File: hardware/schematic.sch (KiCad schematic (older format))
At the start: 21 parts, among them T1 CONN_4, T2 CONN_10, T3 CONN_1, U1 MSP430, U2 LM317

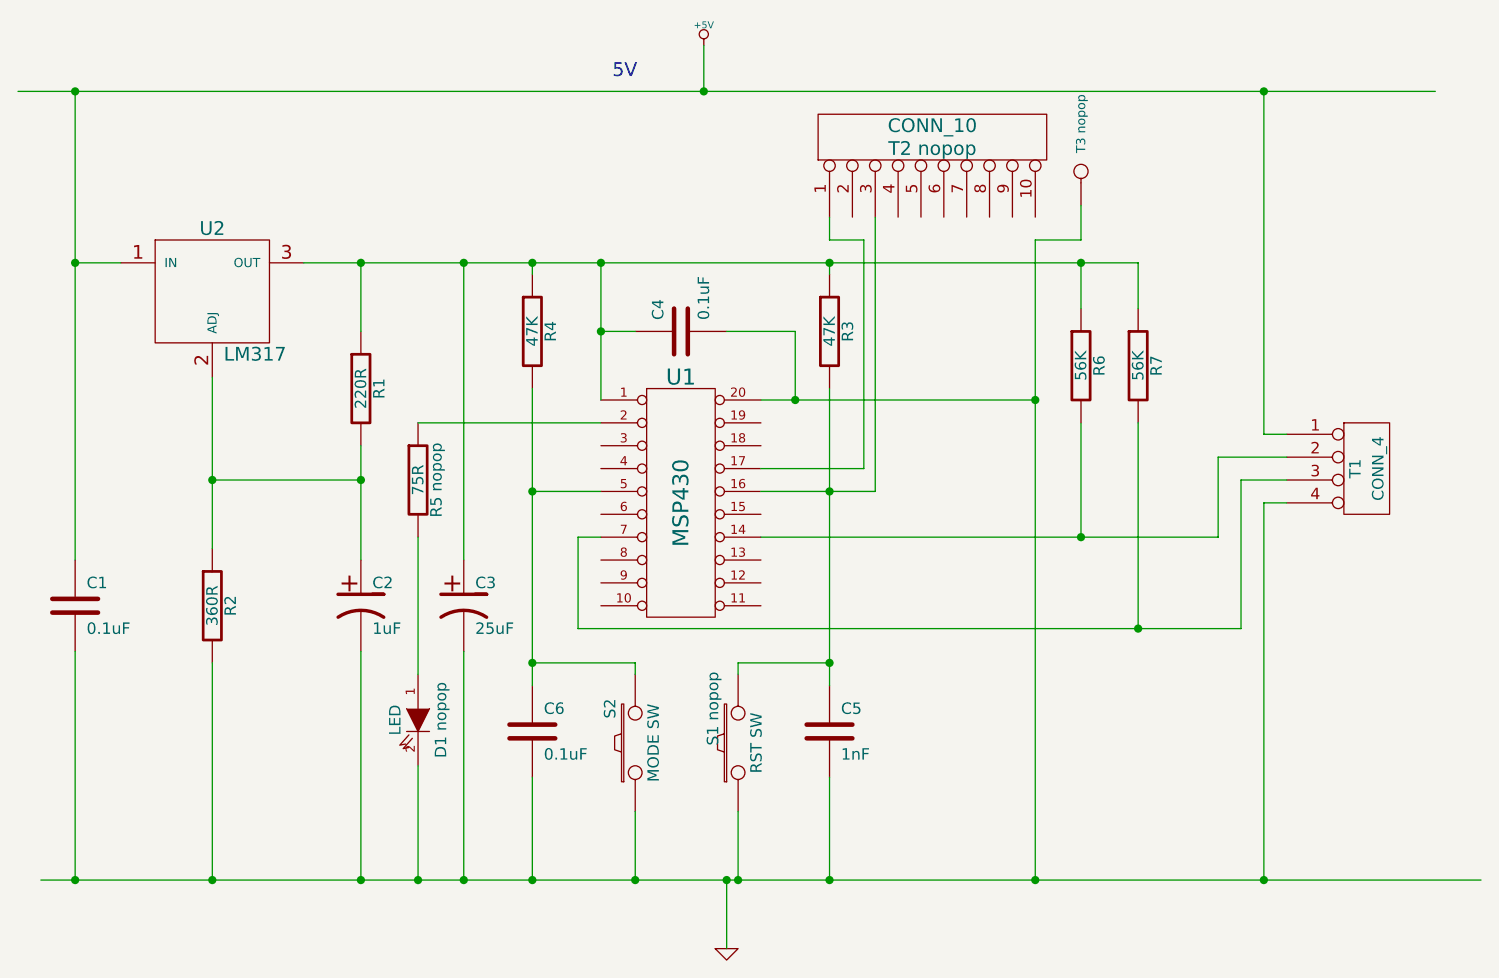
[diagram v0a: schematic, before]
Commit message: Add veroboard Layout
It's a spreadsheet, hardware is now tested and working.
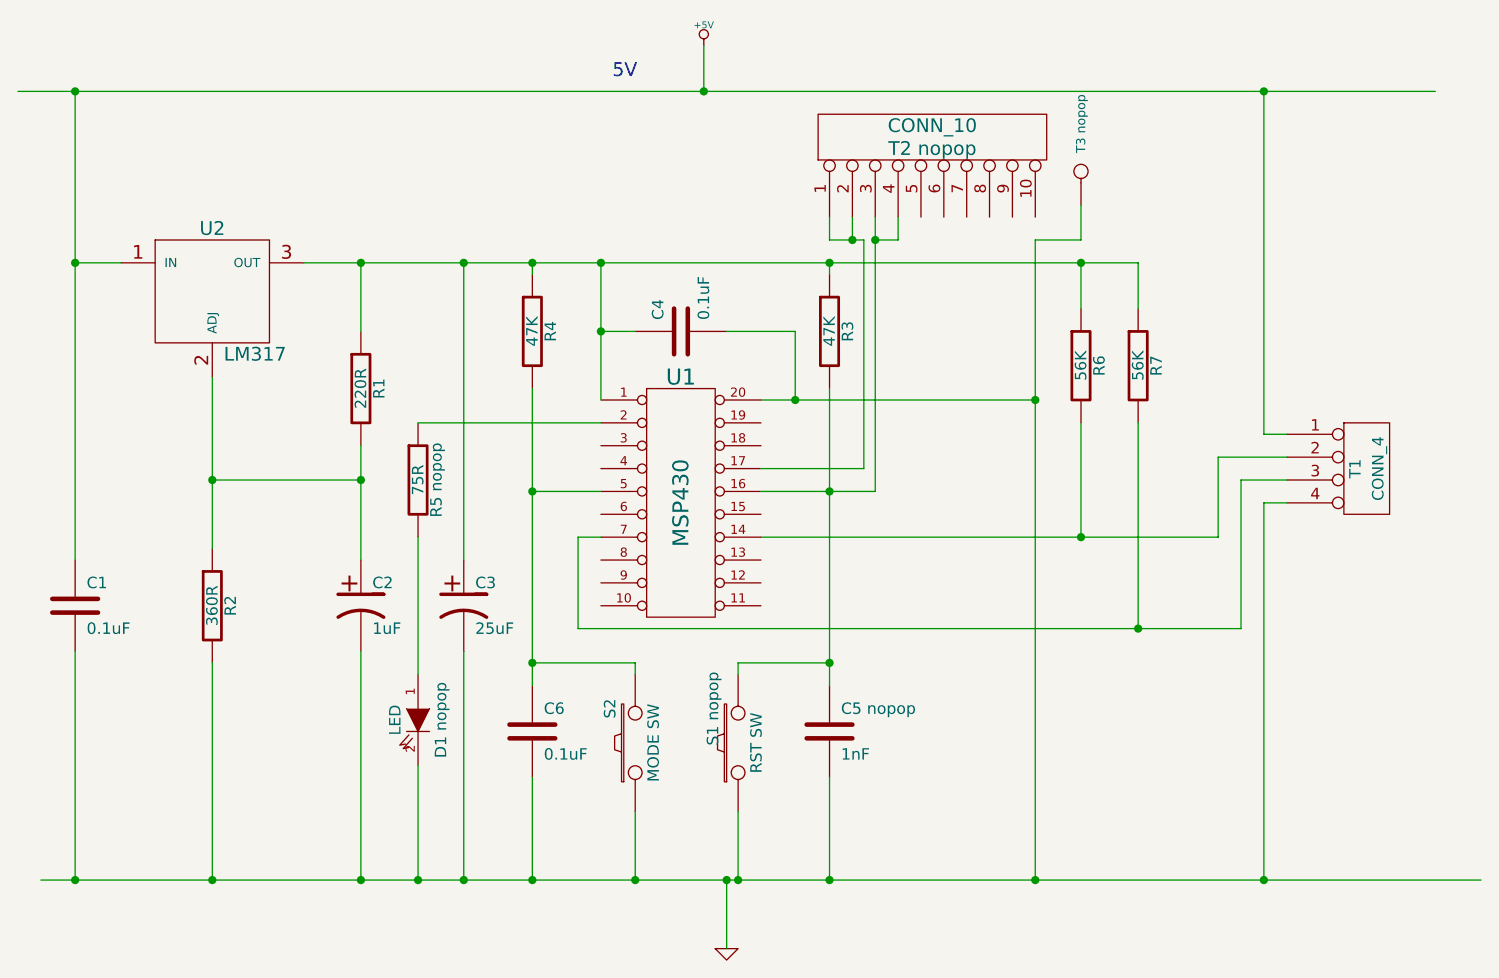
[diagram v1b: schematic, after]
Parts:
- renumbered C5 to C5~nopop, D1 to D1~nopop, R5 to R5~nopop, S1 to S1~nopop, T2 to T2~nopop, T3 to T3~nopop
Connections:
- wire segments 62 -> 65
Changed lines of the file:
@@
-EESchema Schematic File Version 2  date Thu 20 Dec 2012 17:31:51 GMT
+EESchema Schematic File Version 2  date Thu 20 Dec 2012 18:24:55 GMT
 LIBS:power
 LIBS:device
@@
 LIBS:contrib
 LIBS:valves
+LIBS:schematic-cache
 EELAYER 25  0
 EELAYER END
@@
 Comment4 ""
 $EndDescr
+Connection ~ 4650 1500
+Wire Wire Line
+	4650 1500 4750 1500
+Wire Wire Line
+	4750 1500 4750 1400
 Connection ~ 5350 2200
 Wire Wire Line
@@
 Wire Wire Line
 	4600 2500 4150 2500
-$Comp
-L CONN_1 T3
+Wire Wire Line
+	4550 1400 4550 1500
+Connection ~ 4550 1500
+$Comp
+L CONN_1 T3~nopop
 U 1 1 50D343C1
 P 5550 1200
@@
 $EndComp
 $Comp
-L CONN_10 T2
+L CONN_10 T2~nopop
 U 1 1 50D34243
 P 4900 1050
@@
 $EndComp
 $Comp
-L LED D1
+L LED D1~nopop
 U 1 1 50D33CDC
 P 2650 3600
@@
 $EndComp
 $Comp
-L R R5
+L R R5~nopop
 U 1 1 50D33CCD
 P 2650 2550
@@
 $EndComp
 $Comp
-L SW_PUSH S1
+L SW_PUSH S1~nopop
 U 1 1 50D33695
 P 4050 3700
@@
 $EndComp
 $Comp
-L C C5
+L C C5~nopop
 U 1 1 50D334EC
 P 4450 3650
-F 0 "C5" H 4500 3750 50  0000 L CNN
+F 0 "C5 nopop" H 4500 3750 50  0000 L CNN
 F 1 "1nF" H 4500 3550 50  0000 L CNN
 	1    4450 3650
